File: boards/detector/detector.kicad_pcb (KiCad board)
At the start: 2 copper layers, 6 parts, among them J1 ST7920, SW1 Button, U1 ESP32

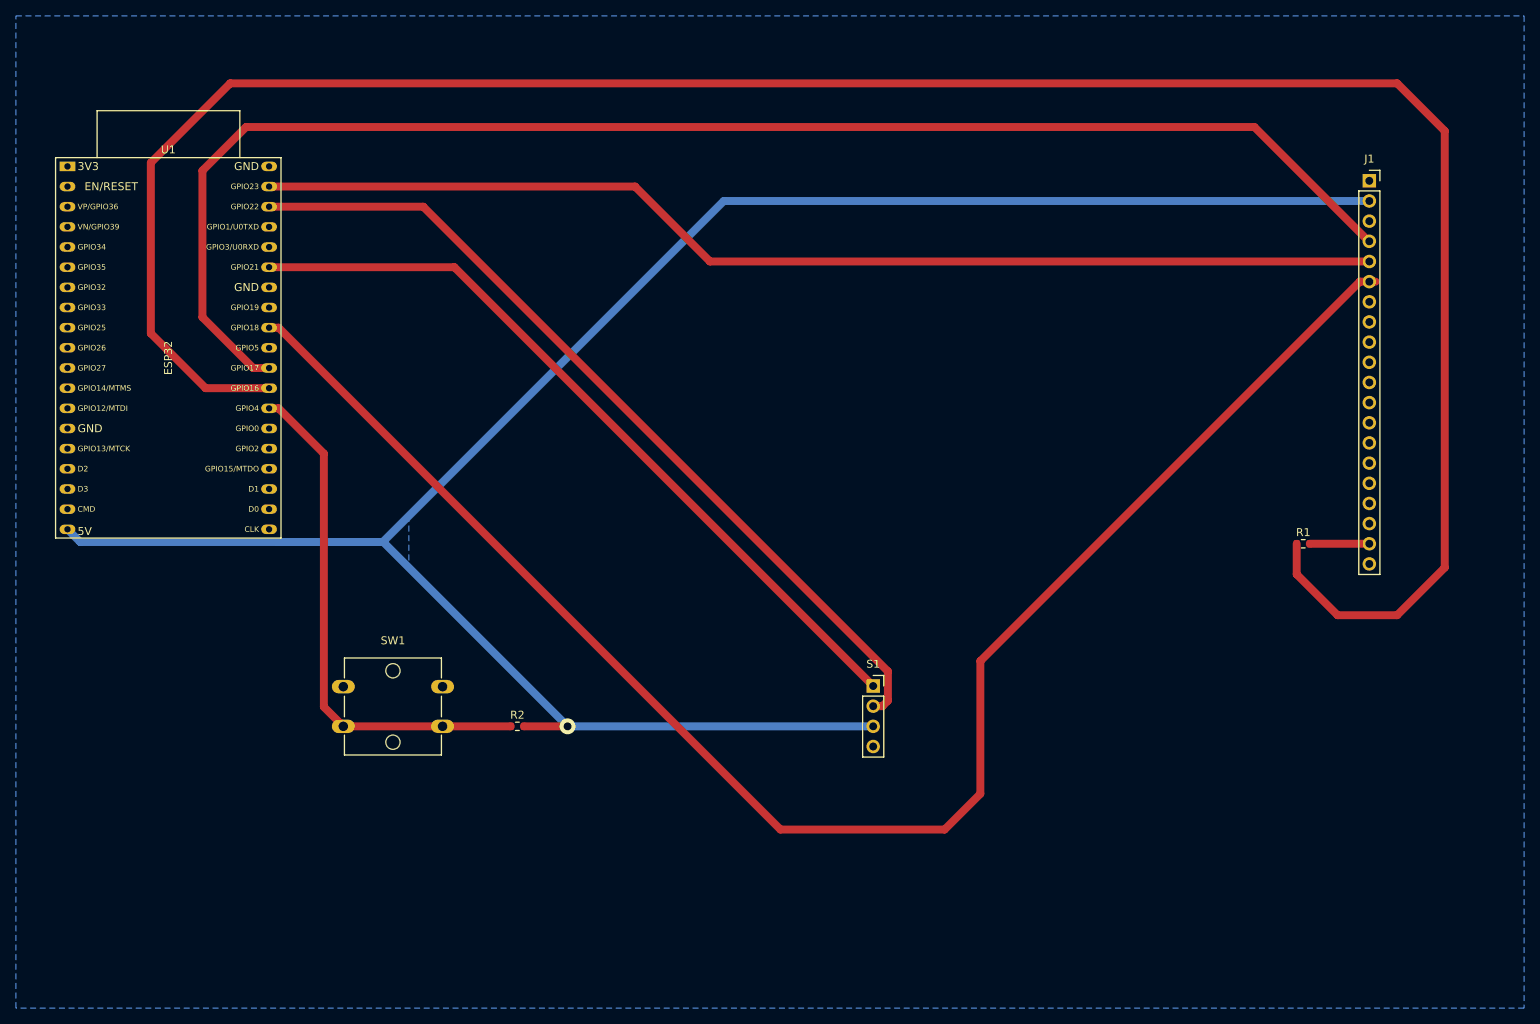
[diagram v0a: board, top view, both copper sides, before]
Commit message: updated detector schematic
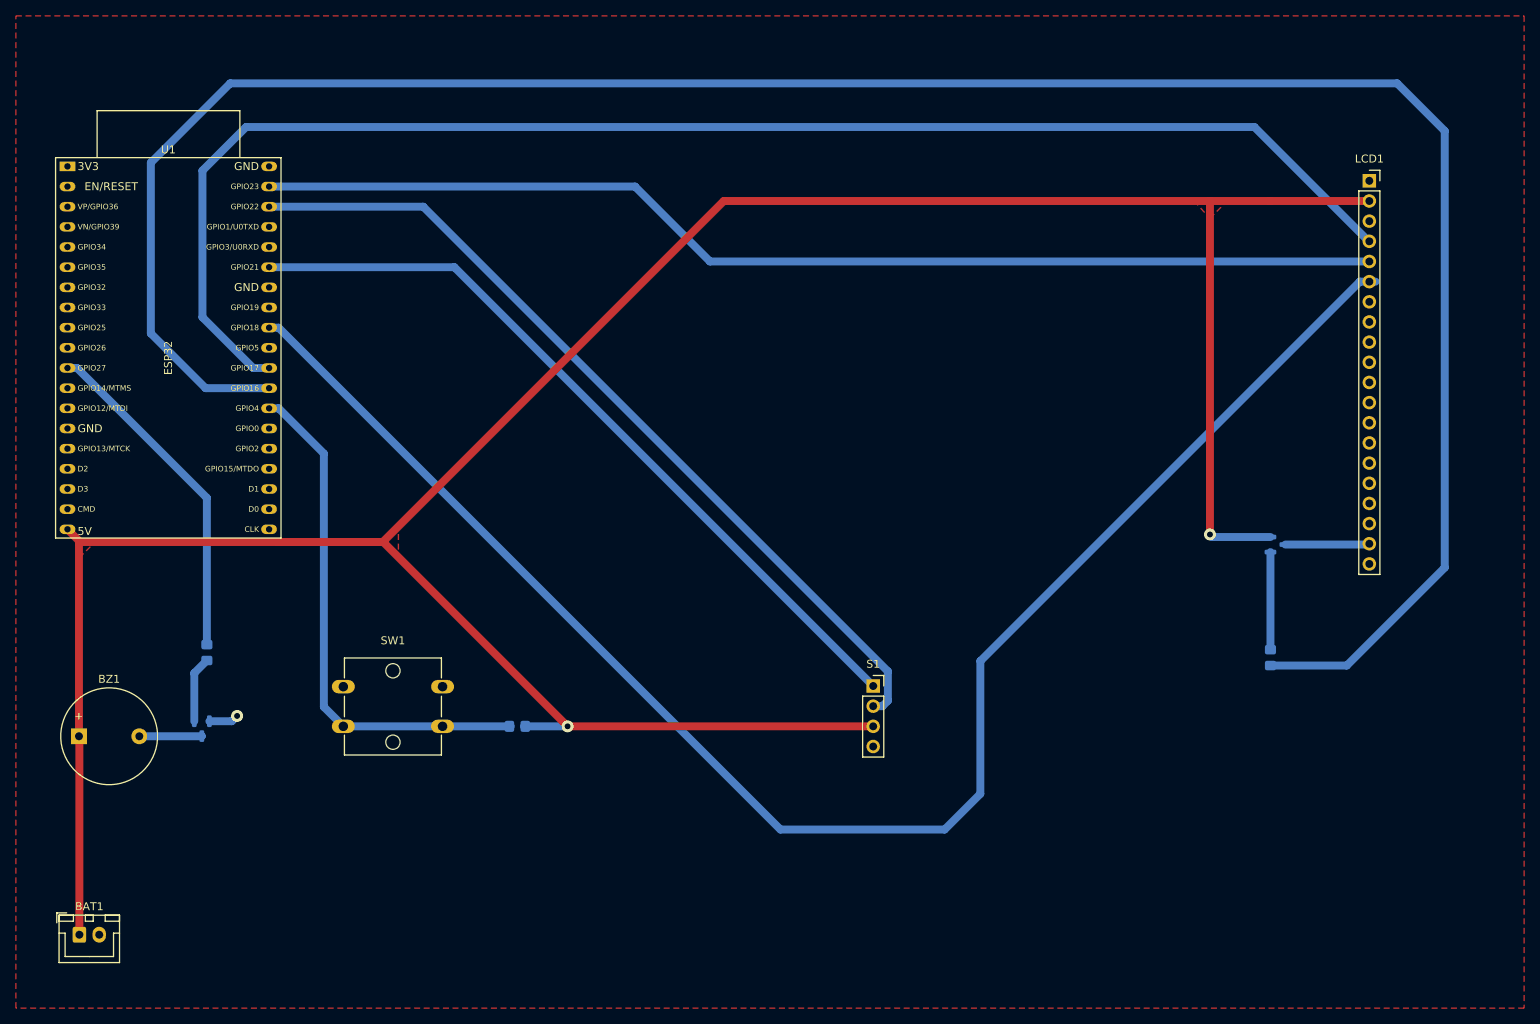
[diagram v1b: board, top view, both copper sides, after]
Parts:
- added BAT1: Battery, Connector_JST:JST_XH_B2B-XH-A_1x02_P2.50mm_Vertical, F.Cu at (83.0, 150.8)
- added BZ1: Buzzer, Buzzer_Beeper:Buzzer_12x9.5RM7.6, F.Cu at (83.0, 125.8)
- added Q1: MMBT3906, Package_TO_SOT_SMD:SOT-23, B.Cu at (234.0, 101.6)
- added Q2: MMBT3904, Package_TO_SOT_SMD:SOT-23, B.Cu at (98.4, 124.8)
- added R3: 1K, Resistor_SMD:R_0805_2012Metric_Pad1.20x1.40mm_HandSolder, B.Cu at (99.1, 115.2)
- R1, R2: footprint Resistor_SMD:R_0603_1608Metric -> Resistor_SMD:R_0805_2012Metric_Pad1.20x1.40mm_HandSolder; moved to B.Cu
- moved R1 14.9 mm to (233.0, 115.8), turned to 90 degrees
- renumbered J1 to LCD1
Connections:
- LCD1 pad 19: Net-(J1-BLA) -> Net-(LCD1-BLA)
- R1 pad 2: Net-(J1-BLA) -> Net-(Q1-B)
- U1 pad 1: +3V3 -> VCC
- U1 pad 11: unconnected-(U1-ADC2_CH7/GPIO27-Pad11) -> /BUZZER
- U1 pad 19: VCC -> unconnected-(U1-5V-Pad19)
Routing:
- net VCC: track 272.6 -> 371.9 mm, vias 1 -> 2
- net /BUZZER: track 0.00 -> 42.8 mm
- net Net-(Q1-B): track 0.00 -> 12.3 mm
- net Net-(LCD1-BLA): track 0.00 -> 10.6 mm
- net Net-(Q2-B): track 0.00 -> 8.31 mm
- net Net-(BZ1--): track 0.00 -> 7.88 mm
- net Net-(J1-BLA): track 7.50 -> 0.00 mm
- net GND: track 0.00 -> 3.77 mm, vias 0 -> 1
- added copper zone on F.Cu, net GND
- added copper zone on F.Cu, net VCC
- removed copper zone on B.Cu, net GND
- removed copper zone on B.Cu, net VCC

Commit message: compacting pcb and fixing sizes
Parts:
- added REF**: MountingHole_2.7mm_M2.5, MountingHole:MountingHole_2.7mm_M2.5, F.Cu at (145.0, 145.0)
- added REF**: MountingHole_2.7mm_M2.5, MountingHole:MountingHole_2.7mm_M2.5, F.Cu at (145.0, 25.0)
- added REF**: MountingHole_2.7mm_M2.5, MountingHole:MountingHole_2.7mm_M2.5, F.Cu at (25.0, 145.0)
- added REF**: MountingHole_2.7mm_M2.5, MountingHole:MountingHole_2.7mm_M2.5, F.Cu at (25.0, 25.0)
- LCD1: footprint Connector_PinSocket_2.54mm:PinSocket_1x20_P2.54mm_Vertical -> Library:ST7920
- moved LCD1 174.9 mm to (72.6, 82.3), turned to 180 degrees
- moved Q1 148.1 mm to (86.5, 88.0)
- moved R1 148.1 mm to (85.6, 102.2)
- moved S1 90.4 mm to (95.1, 98.4)
- moved BAT1 76.7 mm to (36.9, 89.5)
- moved R2 47.1 mm to (91.7, 116.8)
- moved R3 47.1 mm to (52.5, 107.5)
- moved U1 26.0 mm to (61.0, 69.8), turned to 180 degrees
- moved Q2 15.8 mm to (110.5, 135.0)
- moved SW1 10.5 mm to (120.8, 128.9)
- moved BZ1 7.65 mm to (83.8, 133.3)
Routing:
- net VCC: track 371.9 -> 0.00 mm, vias 2 -> 0
- net /BACKLIGHT: track 291.0 -> 0.00 mm
- net /E: track 204.1 -> 0.00 mm
- net /RS: track 184.8 -> 0.00 mm
- net /R/W: track 142.5 -> 0.00 mm
- net /I2C SCL: track 108.0 -> 0.00 mm
- net /I2C SDA: track 98.0 -> 0.00 mm
- net /BUTTON: track 65.7 -> 0.00 mm
- net /BUZZER: track 42.8 -> 0.00 mm
- net Net-(Q1-B): track 12.3 -> 0.00 mm
- net Net-(LCD1-BLA): track 10.6 -> 0.00 mm
- net Net-(Q2-B): track 8.31 -> 0.00 mm
- net Net-(BZ1--): track 7.88 -> 0.00 mm
- net GND: track 3.77 -> 0.00 mm, vias 1 -> 0
- removed copper zone on F.Cu, net GND
- removed copper zone on F.Cu, net VCC
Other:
- board outline added: 130 x 130 mm

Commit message: more work done on the detector board
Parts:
- removed the REF** at (145.0, 145.0)
- removed the REF** at (145.0, 25.0)
- removed the REF** at (25.0, 145.0)
- removed the REF** at (25.0, 25.0)
- added HOLE1: MountingHole_3.2mm_M3, MountingHole:MountingHole_3.2mm_M3, F.Cu at (105.0, 40.0)
- added HOLE3: MountingHole_3.2mm_M3, MountingHole:MountingHole_3.2mm_M3, F.Cu at (105.0, 145.0)
- added HOLE4: MountingHole_3.2mm_M3, MountingHole:MountingHole_3.2mm_M3, F.Cu at (205.0, 145.0)
- added J1: CO, Library:DFRobot Sensor, F.Cu at (146.9, 135.8)
- added J2: Smoke, Library:DFRobot Sensor, F.Cu at (163.7, 135.8)
- added REF**: KiCad-Logo2_12mm_SilkScreen, Symbol:KiCad-Logo2_12mm_SilkScreen, B.Cu at (154.9, 114.3)
- added REF**: OSHW-Logo_19x20mm_SilkScreen, Symbol:OSHW-Logo_19x20mm_SilkScreen, B.Cu at (154.9, 78.7)
- BAT1: footprint Connector_JST:JST_XH_B2B-XH-A_1x02_P2.50mm_Vertical -> Connector_JST:JST_XH_S4B-XH-A_1x04_P2.50mm_Horizontal
- Q1: value MMBT3906 -> MMBT2222A
- Q2: value MMBT3904 -> MMBT2222A
- R1, R2, R3: value 1K -> 10KΩ
- S1: footprint Connector_PinSocket_2.54mm:PinSocket_1x04_P2.54mm_Vertical -> Library:SCD41
- SW1: footprint Button_Switch_THT:SW_SPST_Omron_B3F-40xx -> Library:Button
- moved LCD1 133.7 mm to (205.5, 67.5), turned to 0 degrees
- moved Q1 112.0 mm to (195.9, 111.9), turned to -90 degrees
- moved S1 111.8 mm to (197.0, 144.5), turned to 180 degrees
- moved R1 102.8 mm to (188.0, 111.0), turned to 180 degrees
- moved BAT1 90.7 mm to (113.8, 137.6)
- moved U1 74.4 mm to (131.0, 94.8)
- moved R3 51.5 mm to (104.0, 106.8)
- moved R2 38.0 mm to (129.0, 123.9), turned to -90 degrees
- moved BZ1 30.7 mm to (112.6, 122.8), turned to 180 degrees
- moved Q2 23.2 mm to (105.0, 112.5)
- moved SW1 9.69 mm to (124.1, 119.8), turned to 90 degrees
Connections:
- BAT1 pad 1: VCC -> GND
- BAT1 pad 2: GND -> VCC
- LCD1 pad 18: unconnected-(LCD1-VOUT-Pad18) -> VCC
- LCD1 pad 20: GND -> unconnected-(LCD1-BLK-Pad20)
- Q1 pad 2: VCC -> GND
- R1 pad 1: /BACKLIGHT -> Net-(Q1-B)
- R1 pad 2: Net-(Q1-B) -> /BACKLIGHT
- S1 pad 1: /I2C SDA -> GND
- S1 pad 2: /I2C SCL -> VCC
- S1 pad 3: VCC -> /I2C SCL
- S1 pad 4: GND -> /I2C SDA
- U1 pad 3: unconnected-(U1-SENSOR_VP/GPIO36/ADC1_CH0-Pad3) -> /REF ON
- U1 pad 4: unconnected-(U1-SENSOR_VN/GPIO39/ADC1_CH3-Pad4) -> /REF BAT
- U1 pad 5: unconnected-(U1-VDET_1/GPIO34/ADC1_CH6-Pad5) -> /SMOKE
- U1 pad 6: unconnected-(U1-VDET_2/GPIO35/ADC1_CH7-Pad6) -> /CO
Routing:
- net VCC: track 0.00 -> 232.6 mm, vias 0 -> 1
- net /BACKLIGHT: track 0.00 -> 154.2 mm, vias 0 -> 2
- net /R/W: track 0.00 -> 152.0 mm
- net /E: track 0.00 -> 137.2 mm, vias 0 -> 2
- net /RS: track 0.00 -> 133.1 mm
- net /I2C SDA: track 0.00 -> 124.3 mm, vias 0 -> 3
- net /I2C SCL: track 0.00 -> 119.2 mm, vias 0 -> 3
- net /CO: track 0.00 -> 96.5 mm
- net /BUTTON: track 0.00 -> 69.3 mm, vias 0 -> 2
- net /REF ON: track 0.00 -> 66.8 mm
- net /SMOKE: track 0.00 -> 66.7 mm
- net /REF BAT: track 0.00 -> 60.4 mm
- net /BUZZER: track 0.00 -> 47.1 mm
- net GND: track 0.00 -> 17.3 mm, vias 0 -> 1
- net Net-(LCD1-BLA): track 0.00 -> 9.67 mm
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- added copper zone on F.Cu, net GND
- added copper zone on F.Cu, net VCC
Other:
- board size 130 x 130 mm -> 110 x 115 mm

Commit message: updated pcb to match
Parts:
- removed the REF** at (154.9, 114.3)
- removed the REF** at (154.9, 78.7)
- added R4: 10KΩ, Resistor_SMD:R_0805_2012Metric_Pad1.20x1.40mm_HandSolder, B.Cu at (135.9, 103.9)
- added R5: 10KΩ, Resistor_SMD:R_0805_2012Metric_Pad1.20x1.40mm_HandSolder, B.Cu at (140.8, 103.8)
- added R6: 10KΩ, Resistor_SMD:R_0805_2012Metric_Pad1.20x1.40mm_HandSolder, B.Cu at (149.0, 118.0)
- added R7: 10KΩ, Resistor_SMD:R_0805_2012Metric_Pad1.20x1.40mm_HandSolder, B.Cu at (145.5, 118.0)
- added REF**: OSHW-Symbol_13.4x12mm_SilkScreen, Symbol:OSHW-Symbol_13.4x12mm_SilkScreen, B.Cu at (177.8, 101.6)
- BZ1: footprint Buzzer_Beeper:Buzzer_12x9.5RM7.6 -> Buzzer_Beeper:Buzzer_TDK_PS1240P02BT_D12.2mm_H6.5mm
- moved LCD1 0.74 mm to (205.5, 68.2)
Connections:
- BAT1 pad 3: /REF ON -> Net-(BAT1-Pin_3)
- BAT1 pad 4: /REF BAT -> Net-(BAT1-Pin_4)
- LCD1 pad 18: VCC -> unconnected-(LCD1-VOUT-Pad18)
- LCD1 pad 19: Net-(LCD1-BLA) -> VCC
- LCD1 pad 20: unconnected-(LCD1-BLK-Pad20) -> Net-(LCD1-BLK)
- Q1 pad 3: Net-(LCD1-BLA) -> Net-(LCD1-BLK)
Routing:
- net Net-(BAT1-Pin_4): track 0.00 -> 39.5 mm
- net Net-(BAT1-Pin_3): track 0.00 -> 34.7 mm
- net /REF ON: track 66.8 -> 37.3 mm
- net GND: track 17.3 -> 29.9 mm, vias 1 -> 2
- net Net-(LCD1-BLK): track 0.00 -> 10.8 mm
- net Net-(LCD1-BLA): track 9.67 -> 0.00 mm
- net /REF BAT: track 60.4 -> 57.9 mm
- net VCC: track 232.6 -> 233.4 mm
- net /SMOKE: track 66.7 -> 67.4 mm
- added copper zone on B.Cu, net /REF ON
- added copper zone on B.Cu, net GND
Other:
- board text added: "${TITLE} ${ISSUE_DATE} ${REVISION}"
- board text added: "CALDAS"

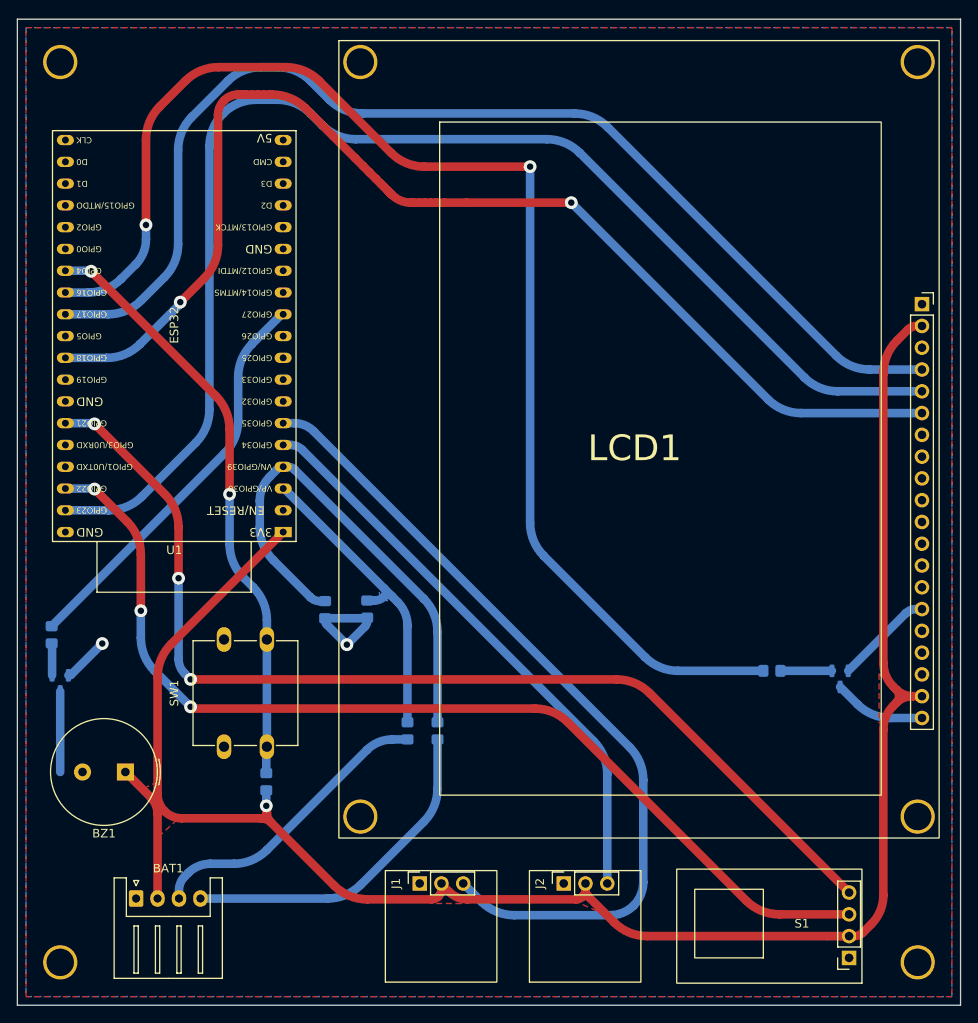
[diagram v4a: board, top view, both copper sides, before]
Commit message: mirrored pcb
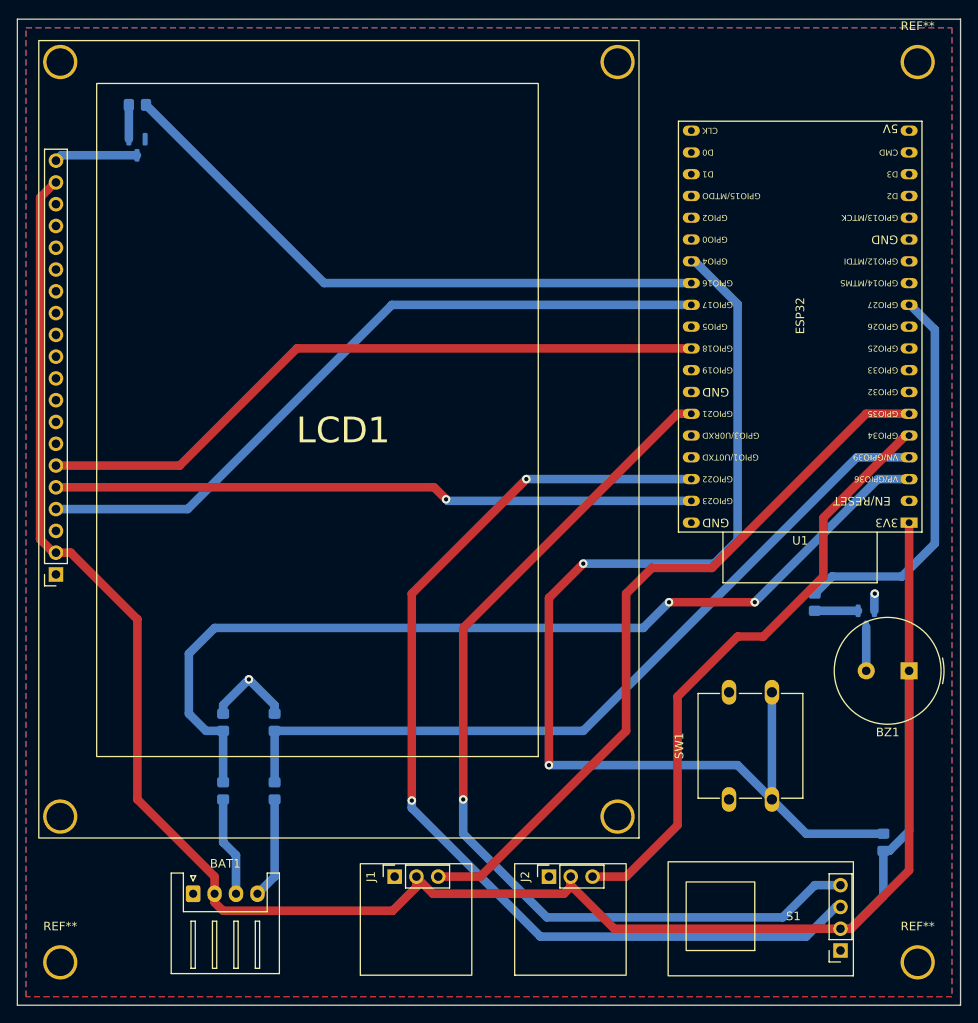
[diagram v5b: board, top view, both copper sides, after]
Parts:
- removed HOLE1, HOLE3, HOLE4: MountingHole_3.2mm_M3, MountingHole:MountingHole_3.2mm_M3
- added REF**: Hole, Library:Hole, F.Cu at (205.0, 145.0)
- added REF**: Hole, Library:Hole, F.Cu at (105.0, 145.0)
- added REF**: Hole, Library:Hole, F.Cu at (205.0, 40.0)
- moved LCD1 105.8 mm to (104.5, 99.8), turned to 180 degrees
- moved Q1 102.8 mm to (114.0, 49.9)
- moved R1 99.2 mm to (114.0, 45.0), turned to 0 degrees
- moved Q2 94.3 mm to (199.0, 104.9)
- moved BZ1 92.2 mm to (204.0, 111.0)
- moved R3 89.1 mm to (193.0, 103.0)
- moved U1 73.0 mm to (204.0, 93.7)
- moved R2 72.3 mm to (201.0, 131.0)
- moved SW1 59.2 mm to (183.0, 126.0)
- moved REF** 47.6 mm to (137.0, 77.0)
- moved R7 22.6 mm to (124.0, 125.0)
- moved R5 21.4 mm to (124.0, 117.0), turned to -90 degrees
- moved R6 20.2 mm to (130.0, 125.0)
- moved R4 14.4 mm to (130.0, 117.0), turned to -90 degrees
- moved BAT1 6.67 mm to (120.5, 137.0)
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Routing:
- net /BACKLIGHT: track 154.2 -> 72.2 mm, vias 2 -> 0
- net /R/W: track 152.3 -> 74.8 mm, vias 0 -> 1
- net /REF ON: track 37.3 -> 110.3 mm, vias 0 -> 2
- net /BUTTON: track 69.3 -> 134.1 mm
- net /E: track 137.5 -> 79.8 mm, vias 2 -> 0
- net /RS: track 133.4 -> 84.0 mm
- net /REF BAT: track 57.9 -> 93.2 mm
- net VCC: track 233.4 -> 261.5 mm, vias 1 -> 0
- net Net-(BAT1-Pin_4): track 39.5 -> 11.8 mm
- net Net-(BAT1-Pin_3): track 34.7 -> 11.6 mm
- net GND: track 29.9 -> 12.5 mm
- net /I2C SDA: track 124.3 -> 110.5 mm, vias 3 -> 1
- net /CO: track 96.5 -> 86.7 mm
- net Net-(BZ1--): track 9.40 -> 5.12 mm
- net /SMOKE: track 67.4 -> 71.0 mm
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- removed copper zone on B.Cu, net /REF ON
- removed copper zone on F.Cu, net VCC

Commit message: updated schematic
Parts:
- removed the REF** at (137.0, 77.0)
- added REF**: OSHW-Symbol_6.7x6mm_SilkScreen, Symbol:OSHW-Symbol_6.7x6mm_SilkScreen, B.Cu at (195.5, 41.2)
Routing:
- net GND: track 12.5 -> 2.02 mm, vias 2 -> 1
- net VCC: track 261.5 -> 257.3 mm
- net /REF BAT: track 93.2 -> 96.5 mm
- net /SMOKE: track 71.0 -> 69.4 mm
- net /CO: track 86.7 -> 85.1 mm
- net /BUTTON: track 134.1 -> 132.6 mm
- net /I2C SDA: track 110.5 -> 109.3 mm
- net /BUZZER: track 45.6 -> 44.6 mm
- net /I2C SCL: track 120.8 -> 119.9 mm
- net /RS: track 84.0 -> 83.4 mm
- net /E: track 79.8 -> 79.2 mm
- added copper zone on F.Cu, net VCC
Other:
- board text added: "${COMPANY} ${TITLE} ${ISSUE_DATE} ${REVISION}"
- board text removed: "${TITLE} ${ISSUE_DATE} ${REVISION}"
- board text removed: "CALDAS"
